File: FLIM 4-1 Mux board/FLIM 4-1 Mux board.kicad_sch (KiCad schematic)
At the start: 83 parts, among them J1 Conn_01x14_Pin, J10 Conn_01x03_Socket, J11 Conn_01x03_Socket, J12 Conn_01x03_Socket, J13 Conn_01x03_Socket, J14 Conn_01x03_Pin, J15 Conn_01x03_Pin, J16 Conn_01x03_Pin, J17 Conn_01x03_Pin, J2 Conn_01x14_Pin, J3 Conn_01x05_Pin, J4 Conn_Coaxial, J5 Conn_Coaxial, J6 Conn_Coaxial, J7 Conn_Coaxial, J8 Conn_Coaxial, J9 Barrel_Jack, SW1 SW_Push_LED, SW2 SW_Push_LED, SW3 SW_Push_LED, SW4 SW_Push_LED, U1 SPDT RF switch, U2 74AHCT74D_118, U3 ADM7150ARDZ-5.0, U4 Itsy_Bitsy_32u4, U5 SPDT RF switch, U6 SPDT RF switch, U7 74AHCT74D_118

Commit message: Add RJ45
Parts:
- removed J1: Conn_01x14_Pin, symbol Connector:Conn_01x14_Pin
- removed R14, R15, R17, R18: 1k, Resistor_SMD:R_0603_1608Metric, symbol Device:R_Small
- added C36: 8.2 nF, Capacitor_SMD:C_0402_1005Metric, symbol Device:C_Small
- added J18: RJ45_Shielded, Custom:AMPHENOL_RJE3A1886102N, symbol Connector:RJ45_Shielded
- added JP1: Jumper_2_Bridged, Jumper:SolderJumper-2_P1.3mm_Bridged_RoundedPad1.0x1.5mm, symbol Jumper:Jumper_2_Bridged
- added RN2: 10k, Resistor_SMD:R_Array_Convex_4x0603, symbol Device:R_Pack04
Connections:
- net CLK: now also RN2.8 (R1.2); no longer RN1.1 (R1.1)
- net D1: now also RN2.5 (R4.2)
- net D1*: now also J18.7
- net D2: now also RN2.6 (R3.2)
- net D2*: now also J18.5
- net D3: now also RN2.7 (R2.2)
- net D3*: now also J18.3
- net GND: now also C36.2, J18.2, J18.4, J18.6, J18.8, JP1.1 (A), RN2.1 (R1.1), RN2.2 (R2.1), RN2.3 (R3.1), RN2.4 (R4.1)
- new net: C36.1, J18.SH, JP1.2 (B)
- new net CLK*: J18.1, RN1.1 (R1.1)
- no-connect marks 12 -> 10

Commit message: add missing header
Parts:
- added J19: Conn_01x14_Pin, symbol Connector:Conn_01x14_Pin
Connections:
- no-connect marks 10 -> 12
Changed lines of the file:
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@@
 	)
 	(no_connect
+		(at 214.122 25.4)
+	)
+	(no_connect
 		(at 248.92 27.94)
 	)
 	(no_connect
+		(at 214.122 27.94)
+	)
+	(no_connect
 		(at 226.06 25.4)
 	)
@@
 					(unit 1)
 				)
+			)
+		)
+	)
+	(symbol
+		(lib_id "Connector:Conn_01x14_Pin")
+		(at 209.042 35.56 0)
+		(unit 1)
+		(body_style 1)
+		(exclude_from_sim no)
+		(in_bom yes)
+		(on_board no)
+		(in_pos_files yes)
+		(dnp no)
+		(property "Reference" "J19"
+			(at 209.677 15.24 0)
+			(show_name no)
+			(do_not_autoplace no)
+			(effects
+				(font
+					(size 1.27 1.27)
+				)
+			)
+		)
+		(property "Value" "Conn_01x14_Pin"
+			(at 209.677 17.78 0)
+			(show_name no)
+			(do_not_autoplace no)
+			(effects
+				(font
+					(size 1.27 1.27)
+				)
+			)
+		)
+		(property "Footprint" ""
+			(at 209.042 35.56 0)
+			(hide yes)
+			(show_name no)
+			(do_not_autoplace no)
+			(effects
+				(font
+					(size 1.27 1.27)
+				)
+			)
+		)
+		(property "Datasheet" "https://suddendocs.samtec.com/catalog_english/tsm.pdf"
+			(at 209.042 35.56 0)
+			(hide yes)
+			(show_name no)
+			(do_not_autoplace no)
+			(effects
+				(font
+					(size 1.27 1.27)
+				)
+			)
+		)
+		(property "Description" "Connector Header Surface Mount 14 position 0.100\" (2.54mm)"
+			(at 209.042 35.56 0)
+			(hide yes)
+			(show_name no)
+			(do_not_autoplace no)
+			(effects
+				(font
+					(size 1.27 1.27)
+				)
+			)
+		)
+		(property "Manufacturer" "Samtec Inc."
+			(at 209.042 35.56 0)
+			(hide yes)
+			(show_name no)
+			(do_not_autoplace no)
+			(effects
+				(font
+					(size 1.27 1.27)
+				)
+			)
+		)
+		(property "Part #" "TSM-114-01-T-SV"
+			(at 209.042 35.56 0)
+			(hide yes)
+			(show_name no)
+			(do_not_autoplace no)
+			(effects
+				(font
+					(size 1.27 1.27)
+				)
+			)
+		)
+		(pin "13"
+		)
+		(pin "7"
+		)
+		(pin "12"
+		)
+		(pin "4"
+		)
+		(pin "8"
+		)
+		(pin "2"
+		)
+		(pin "11"
+		)
+		(pin "3"
+		)
+		(pin "14"
+		)
+		(pin "10"
+		)
+		(pin "9"
+		)
+		(pin "1"
+		)
+		(pin "5"
+		)
+		(pin "6"
+		)
+		(instances
+			(project "FLIM 4-1 Mux board"
+				(path "/9a5ec920-9f12-407d-b06b-b123ad2c0d9b"
+					(reference "J19")
+					(unit 1)
+				)

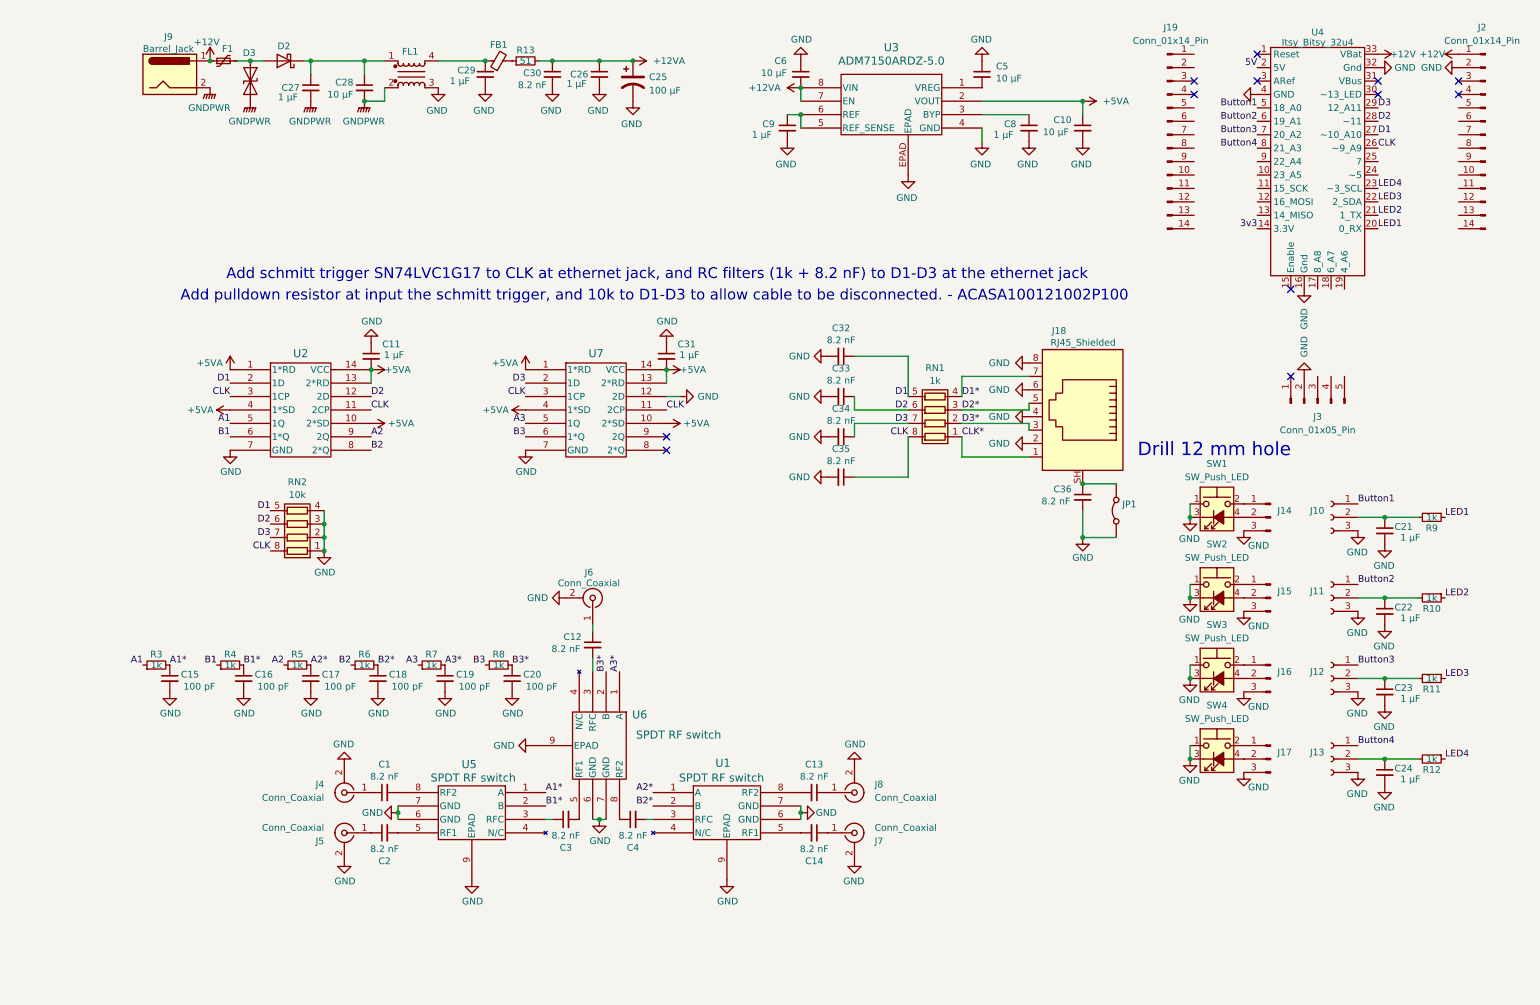
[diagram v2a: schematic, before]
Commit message: Start PCB draft of RF board
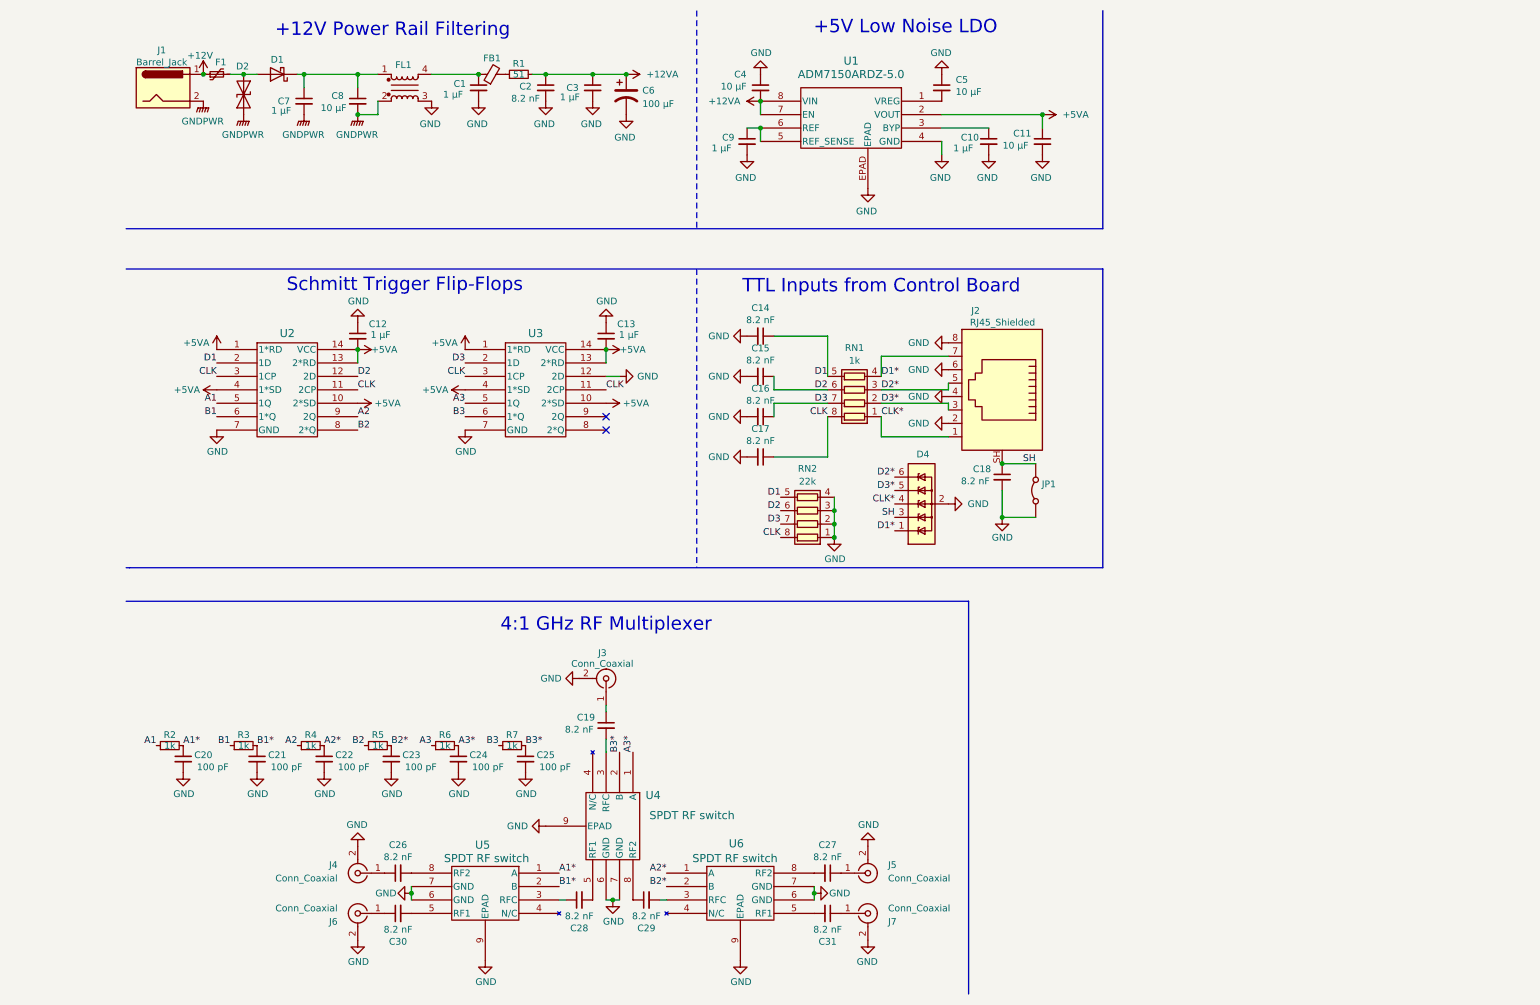
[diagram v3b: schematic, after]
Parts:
- removed C21, C22, C23, C24: 1 µF, Capacitor_SMD:C_0805_2012Metric, symbol Device:C_Small
- removed J10, J11, J12, J13: Conn_01x03_Socket, Connector_PinSocket_2.54mm:PinSocket_1x03_P2.54mm_Vertical_SMD_Pin1Left, symbol Connector:Conn_01x03_Socket
- removed J14, J15, J16, J17: Conn_01x03_Pin, symbol Connector:Conn_01x03_Pin
- removed J19, J2: Conn_01x14_Pin, symbol Connector:Conn_01x14_Pin
- removed J3: Conn_01x05_Pin, symbol Connector:Conn_01x05_Pin
- removed R10, R11, R12, R9: 1k, Resistor_SMD:R_0603_1608Metric, symbol Device:R_Small
- removed SW1, SW2, SW3, SW4: SW_Push_LED, symbol Switch:SW_Push_LED
- removed U4: Itsy_Bitsy_32u4, Custom:Itsy Bitsy 32u4 with headers, symbol custom:Itsy_Bitsy_32u4
- added D4: SMF05CT, Package_TO_SOT_SMD:SOT-363_SC-70-6, symbol Power_Protection:ESDA6V1-5SC6
- C20: renamed from C15; footprint Capacitor_SMD:C_0603_1608Metric -> Capacitor_SMD:C_0402_1005Metric; Manufacturer KEMET -> Walsin Technology Corporation; Part # C0603C101J1GACTU -> MT15N101J500CT
- C21: renamed from C16; footprint Capacitor_SMD:C_0603_1608Metric -> Capacitor_SMD:C_0402_1005Metric; Manufacturer KEMET -> Walsin Technology Corporation; Part # C0603C101J1GACTU -> MT15N101J500CT
- C22: renamed from C17; footprint Capacitor_SMD:C_0603_1608Metric -> Capacitor_SMD:C_0402_1005Metric; Manufacturer KEMET -> Walsin Technology Corporation; Part # C0603C101J1GACTU -> MT15N101J500CT
- C23: renamed from C18; footprint Capacitor_SMD:C_0603_1608Metric -> Capacitor_SMD:C_0402_1005Metric; Manufacturer KEMET -> Walsin Technology Corporation; Part # C0603C101J1GACTU -> MT15N101J500CT
- C24: renamed from C19; footprint Capacitor_SMD:C_0603_1608Metric -> Capacitor_SMD:C_0402_1005Metric; Manufacturer KEMET -> Walsin Technology Corporation; Part # C0603C101J1GACTU -> MT15N101J500CT
- C25: renamed from C20; footprint Capacitor_SMD:C_0603_1608Metric -> Capacitor_SMD:C_0402_1005Metric; Manufacturer KEMET -> Walsin Technology Corporation; Part # C0603C101J1GACTU -> MT15N101J500CT
- R2: renamed from R3; footprint Resistor_SMD:R_0603_1608Metric -> Resistor_SMD:R_0402_1005Metric; Manufacturer Susumu -> Stackpole Electronics Inc
- R3: renamed from R4; footprint Resistor_SMD:R_0603_1608Metric -> Resistor_SMD:R_0402_1005Metric; Manufacturer Susumu -> Stackpole Electronics Inc
- R4: renamed from R5; footprint Resistor_SMD:R_0603_1608Metric -> Resistor_SMD:R_0402_1005Metric; Manufacturer Susumu -> Stackpole Electronics Inc
- R5: renamed from R6; footprint Resistor_SMD:R_0603_1608Metric -> Resistor_SMD:R_0402_1005Metric; Manufacturer Susumu -> Stackpole Electronics Inc
- R6: renamed from R7; footprint Resistor_SMD:R_0603_1608Metric -> Resistor_SMD:R_0402_1005Metric; Manufacturer Susumu -> Stackpole Electronics Inc
- R7: renamed from R8; footprint Resistor_SMD:R_0603_1608Metric -> Resistor_SMD:R_0402_1005Metric; Manufacturer Susumu -> Stackpole Electronics Inc
- RN1: Part # RAVF164DJT1K00 -> RNCP0402FTD1K00
- RN2: value 10k -> 22k; Part # CAY16-1002F4LF -> CAY16-2202F4LF
- renumbered C29 to C1, C8 to C10, C10 to C11, C11 to C12, C31 to C13, C32 to C14, C33 to C15, C34 to C16, C35 to C17, C36 to C18, C12 to C19, C30 to C2, C1 to C26, C13 to C27, C3 to C28, C4 to C29, C26 to C3, C2 to C30, C14 to C31, C6 to C4, C25 to C6, C27 to C7, C28 to C8, D2 to D1, D3 to D2, J9 to J1, J18 to J2, J6 to J3, J8 to J5, J5 to J6, R13 to R1, U3 to U1, U7 to U3, U6 to U4, U1 to U6
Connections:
- net CLK*: now also D4.4 (IO3)
- net D1*: now also D4.1 (IO1)
- net D2*: now also D4.6 (IO5)
- net D3*: now also D4.5 (IO4)
- net GND: now also D4.2 (GND)
- net SH: now reaches C18.1, J2.SH, JP1.2 (B)
- net SH: now also D4.3 (IO2)
- no-connect marks 12 -> 2
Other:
- note added: "+12V Power Rail Filtering"
- note added: "+5V Low Noise LDO"
- note added: "4:1 GHz RF Multiplexer"
- note added: "Schmitt Trigger Flip-Flops"
- note added: "TTL Inputs from Control Board"
- note removed: "Add pulldown resistor at input the schmitt trigger, and 10k to D1-D3 to allow cable to be disconnected. - ACASA100121002P100"
- note removed: "Add schmitt trigger SN74LVC1G17 to CLK at ethernet jack, and RC filters (1k + 8.2 nF) to D1-D3 at the ethernet jack"
- note removed: "Drill 12 mm hole"
- moved on the sheet: C1, C10, C11, C12, C13, C14, C15, C16, C17, C18, C19, C2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

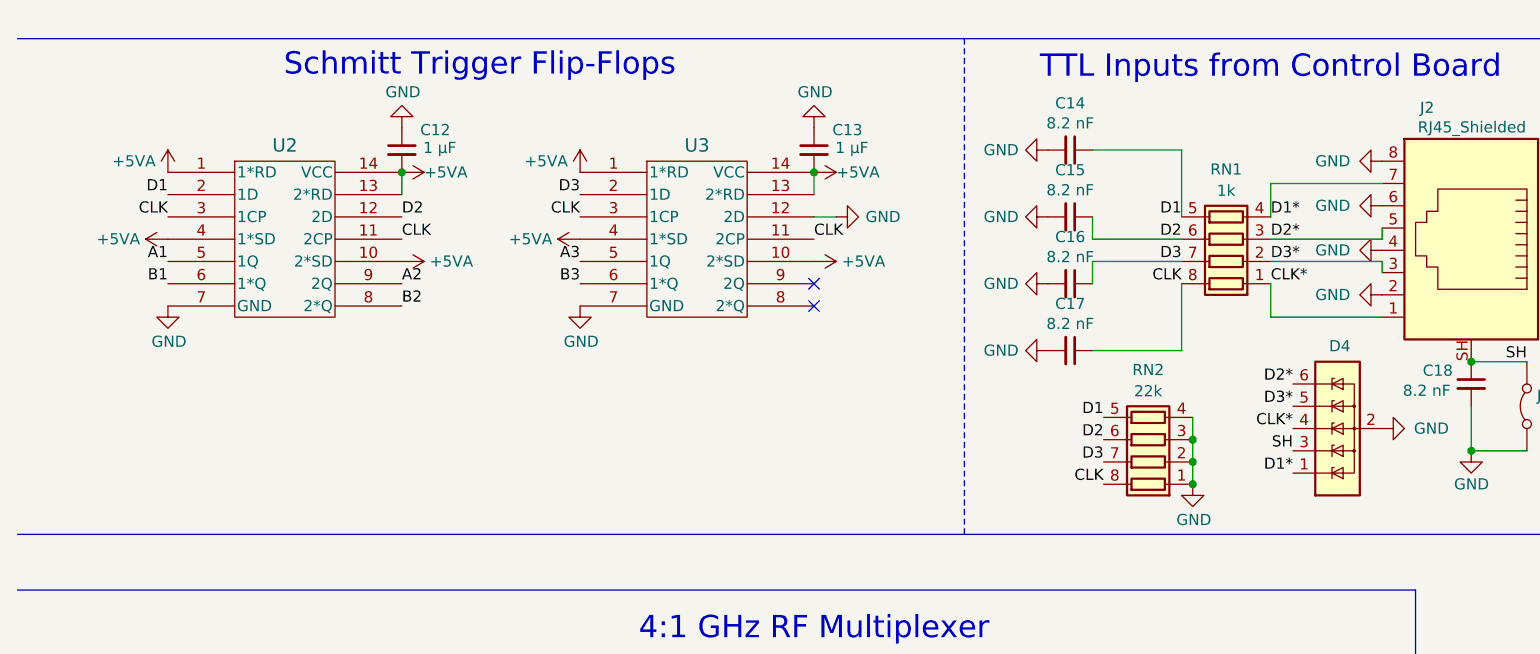
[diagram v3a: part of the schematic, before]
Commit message: Finished working draft of PCB - passes DRC
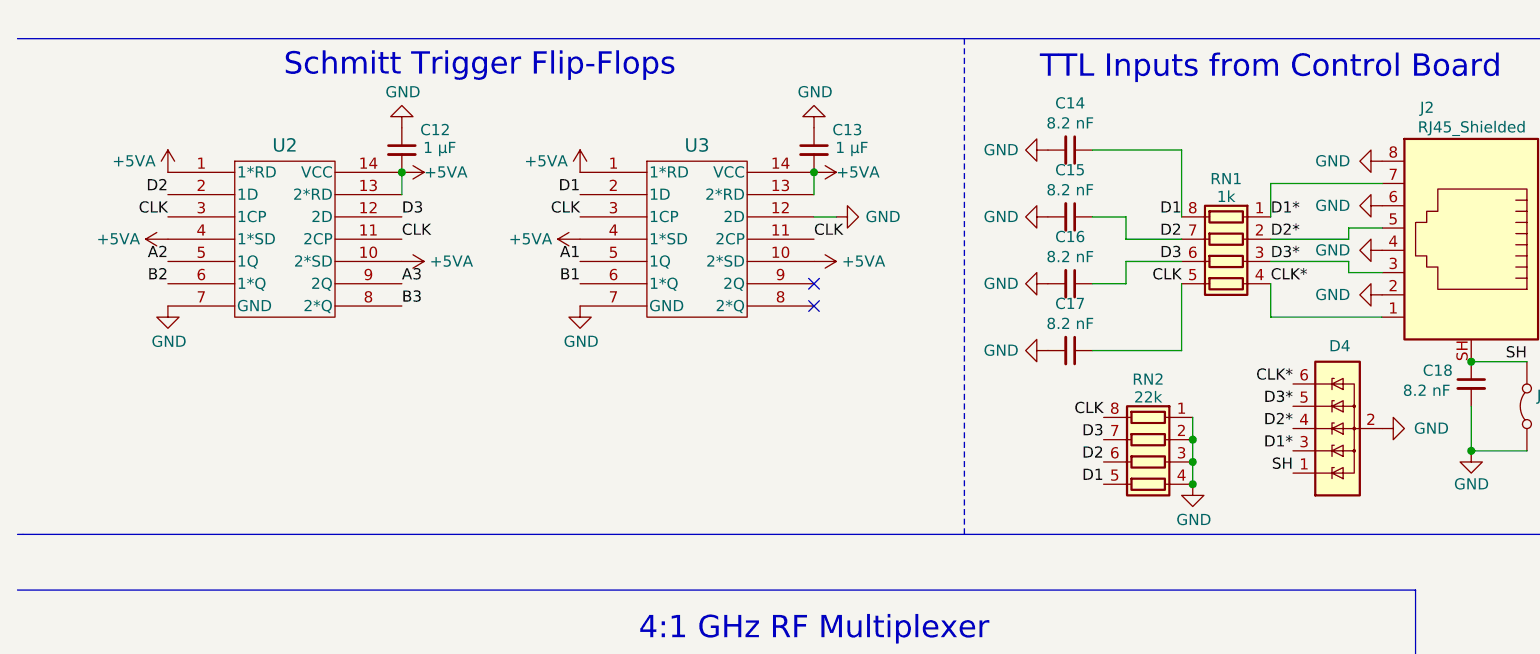
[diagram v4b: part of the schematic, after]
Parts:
- R2, R3, R4, R5, R6, R7: Part # RG1608P-102-B-T5 -> RNCP0402FTD1K00
- RN1: Manufacturer Stackpole Electronics Inc -> Bourns Inc.; Part # RNCP0402FTD1K00 -> CAY16-1001F4LF
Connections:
- net A1: now also U3.5 (1Q); no longer U2.5 (1Q)
- net A2: now also U2.5 (1Q); no longer U2.9 (2Q)
- net A3: now also U2.9 (2Q); no longer U3.5 (1Q)
- net B1: now also U3.6 (1*Q); no longer U2.6 (1*Q)
- net B2: now also U2.6 (1*Q); no longer U2.8 (2*Q)
- net B3: now also U2.8 (2*Q); no longer U3.6 (1*Q)
- net CLK: now also RN1.5 (R4.2); no longer RN1.8 (R1.2)
- net CLK*: now also D4.6 (IO5), RN1.4 (R4.1); no longer D4.4 (IO3), RN1.1 (R1.1)
- net D1: now also RN1.8 (R1.2), U3.2 (1D); no longer RN1.5 (R4.2), U2.2 (1D)
- net D1*: now also D4.3 (IO2), RN1.1 (R1.1); no longer D4.1 (IO1), RN1.4 (R4.1)
- net D2: now also RN1.7 (R2.2), U2.2 (1D); no longer RN1.6 (R3.2), U2.12 (2D)
- net D2*: now also D4.4 (IO3), RN1.2 (R2.1); no longer D4.6 (IO5), RN1.3 (R3.1)
- net D3: now also RN1.6 (R3.2), U2.12 (2D); no longer RN1.7 (R2.2), U3.2 (1D)
- net D3*: now also RN1.3 (R3.1); no longer RN1.2 (R2.1)
- net SH: now also D4.1 (IO1); no longer D4.3 (IO2)

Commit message: Untested Impedance matching taper on SMA pins
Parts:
- added SYM1: Logo_Open_Hardware_Small, Symbol:OSHW-Logo_5.7x6mm_SilkScreen, symbol Graphic:Logo_Open_Hardware_Small
- added SYM2: Logo_Open_Hardware_Small, Custom:CC-BY-SA Symbol, symbol Graphic:Logo_Open_Hardware_Small
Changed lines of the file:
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@@
+	)
+	(symbol
+		(lib_id "Graphic:Logo_Open_Hardware_Small")
+		(at 204.47 129.54 0)
+		(unit 1)
+		(body_style 1)
+		(exclude_from_sim no)
+		(in_bom no)
+		(on_board yes)
+		(in_pos_files yes)
+		(dnp no)
+		(fields_autoplaced yes)
+		(property "Reference" "SYM2"
+			(at 204.47 122.555 0)
+			(hide yes)
+			(show_name no)
+			(do_not_autoplace no)
+			(effects
+				(font
+					(size 1.27 1.27)
+				)
+			)
+		)
+		(property "Value" "Logo_Open_Hardware_Small"
+			(at 204.47 135.255 0)
+			(hide yes)
+			(show_name no)
+			(do_not_autoplace no)
+			(effects
+				(font
+					(size 1.27 1.27)
+				)
+			)
+		)
+		(property "Footprint" "Custom:CC-BY-SA Symbol"
+			(at 204.47 129.54 0)
+			(hide yes)
+			(show_name no)
+			(do_not_autoplace no)
+			(effects
+				(font
+					(size 1.27 1.27)
+				)
+			)
+		)
+		(property "Datasheet" ""
+			(at 204.47 129.54 0)
+			(hide yes)
+			(show_name no)
+			(do_not_autoplace no)
+			(effects
+				(font
+					(size 1.27 1.27)
+				)
+			)
+		)
+		(property "Description" "Open Hardware logo, small"
+			(at 204.47 129.54 0)
+			(hide yes)
+			(show_name no)
+			(do_not_autoplace no)
+			(effects
+				(font
+					(size 1.27 1.27)
+				)
+			)
+		)
+		(property "Sim.Enable" "0"
+			(at 204.47 129.54 0)
+			(hide yes)
+			(show_name no)
+			(do_not_autoplace no)
+			(effects
+				(font
+					(size 1.27 1.27)
+				)
+			)
+		)
+		(property "Manufacturer" ""
+			(at 204.47 129.54 0)
+			(hide yes)
+			(show_name no)
+			(do_not_autoplace no)
+			(effects
+				(font
+					(size 1.27 1.27)
+				)
+			)
+		)
+		(instances
+			(project "FLIM 4-1 Mux board"
+				(path "/9a5ec920-9f12-407d-b06b-b123ad2c0d9b"
+					(reference "SYM2")
+					(unit 1)
+				)
+			)
+		)
 	)
 	(symbol
@@
 					(unit 1)
 				)
+			)
+		)
+	)
+	(symbol
+		(lib_id "Graphic:Logo_Open_Hardware_Small")
+		(at 190.5 129.54 0)
+		(unit 1)
+		(body_style 1)
+		(exclude_from_sim no)
+		(in_bom no)
+		(on_board yes)
+		(in_pos_files yes)
+		(dnp no)
+		(fields_autoplaced yes)
+		(property "Reference" "SYM1"
+			(at 190.5 122.555 0)
+			(hide yes)
+			(show_name no)
+			(do_not_autoplace no)
+			(effects
+				(font
+					(size 1.27 1.27)
+				)
+			)
+		)
+		(property "Value" "Logo_Open_Hardware_Small"
+			(at 190.5 135.255 0)
+			(hide yes)
+			(show_name no)
+			(do_not_autoplace no)
+			(effects
+				(font
+					(size 1.27 1.27)
+				)
+			)
+		)
+		(property "Footprint" "Symbol:OSHW-Logo_5.7x6mm_SilkScreen"
+			(at 190.5 129.54 0)
+			(hide yes)
+			(show_name no)
+			(do_not_autoplace no)
+			(effects
+				(font
+					(size 1.27 1.27)
+				)
+			)
+		)
+		(property "Datasheet" ""
+			(at 190.5 129.54 0)
+			(hide yes)
+			(show_name no)
+			(do_not_autoplace no)
+			(effects
+				(font
+					(size 1.27 1.27)
+				)
+			)
+		)
+		(property "Description" "Open Hardware logo, small"
+			(at 190.5 129.54 0)
+			(hide yes)
+			(show_name no)
+			(do_not_autoplace no)
+			(effects
+				(font
+					(size 1.27 1.27)
+				)
+			)
+		)
+		(property "Sim.Enable" "0"
+			(at 190.5 129.54 0)
+			(hide yes)
+			(show_name no)
+			(do_not_autoplace no)
+			(effects
+				(font
+					(size 1.27 1.27)
+				)
+			)
+		)
+		(property "Manufacturer" ""
+			(at 190.5 129.54 0)
+			(hide yes)
+			(show_name no)
+			(do_not_autoplace no)
+			(effects
+				(font
+					(size 1.27 1.27)
+				)
+			)
+		)
+		(instances
+			(project "FLIM 4-1 Mux board"
+				(path "/9a5ec920-9f12-407d-b06b-b123ad2c0d9b"
+					(reference "SYM1")
+					(unit 1)
+				)
